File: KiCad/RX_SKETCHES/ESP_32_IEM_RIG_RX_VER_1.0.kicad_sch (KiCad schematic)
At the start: 0 parts

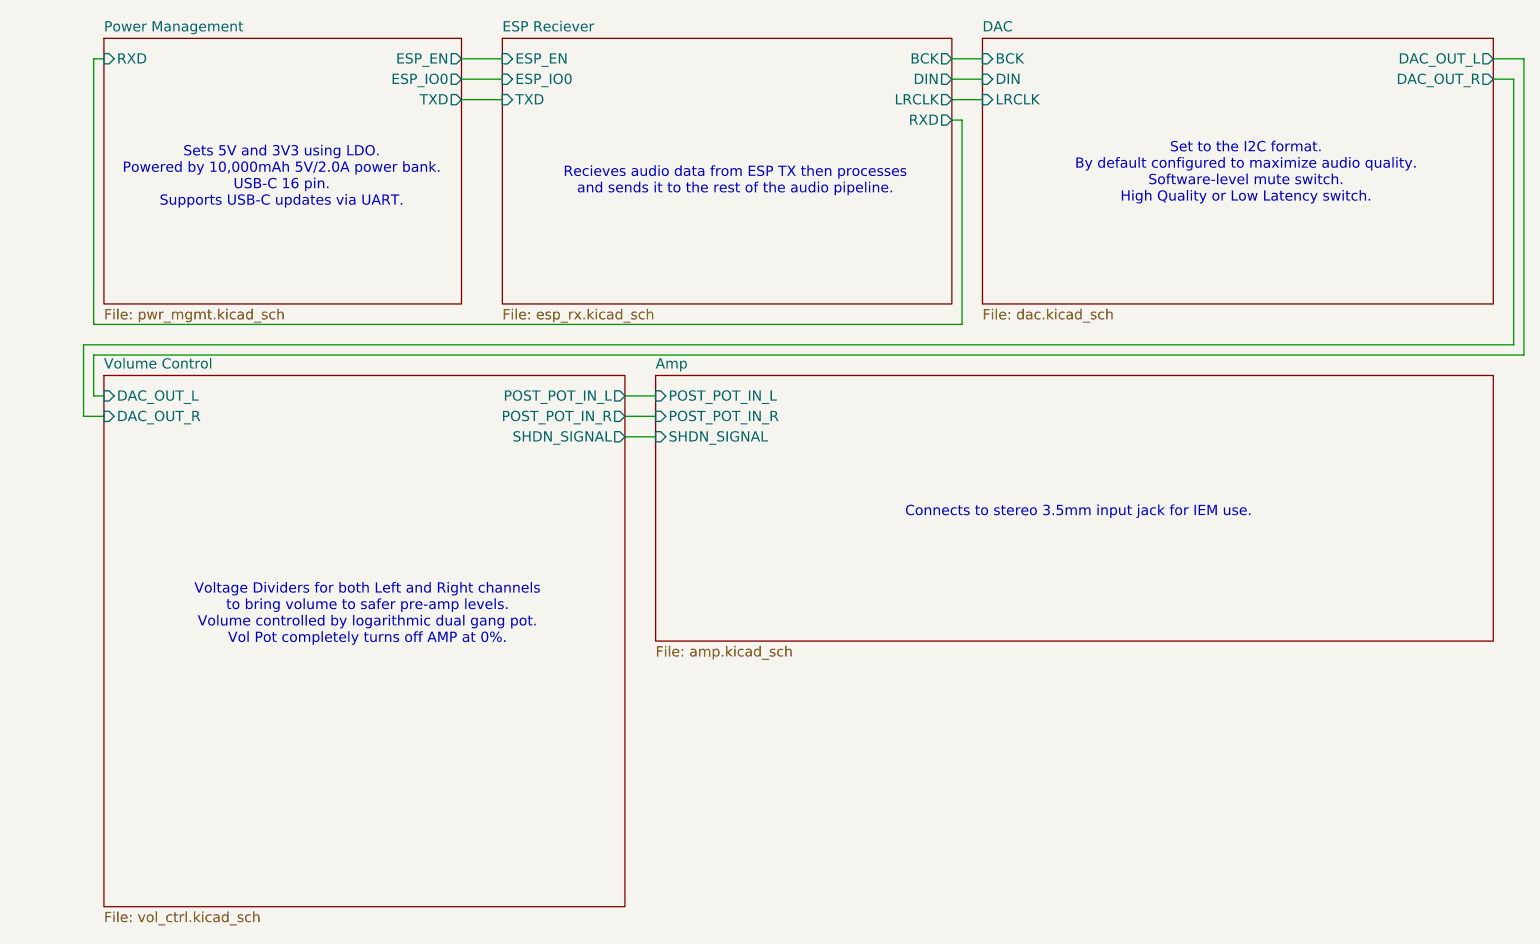
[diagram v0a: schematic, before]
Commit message: Rewire RX hierarchical labels and mark proto DNP parts.
Keep the rotated WROOM-32U and breadboard I2S GPIOs, but attach
ESP_EN/IO0, UART, and BCK/DIN/LRCLK to the pins that actually sit
there after the 270° rotate. Move PCM5102 I2S off FMT/DEMP/XSMT,
put amp shutdown on ~{SHDN}, keep the datasheet 470R+2.2nF filter,
DNP the experimental pot pad and MAX97220A input resistors, and
switch schematic passives to 0805 for hand assembly.

Co-authored-by: luciano <dlmuschamp@users.noreply.github.com>
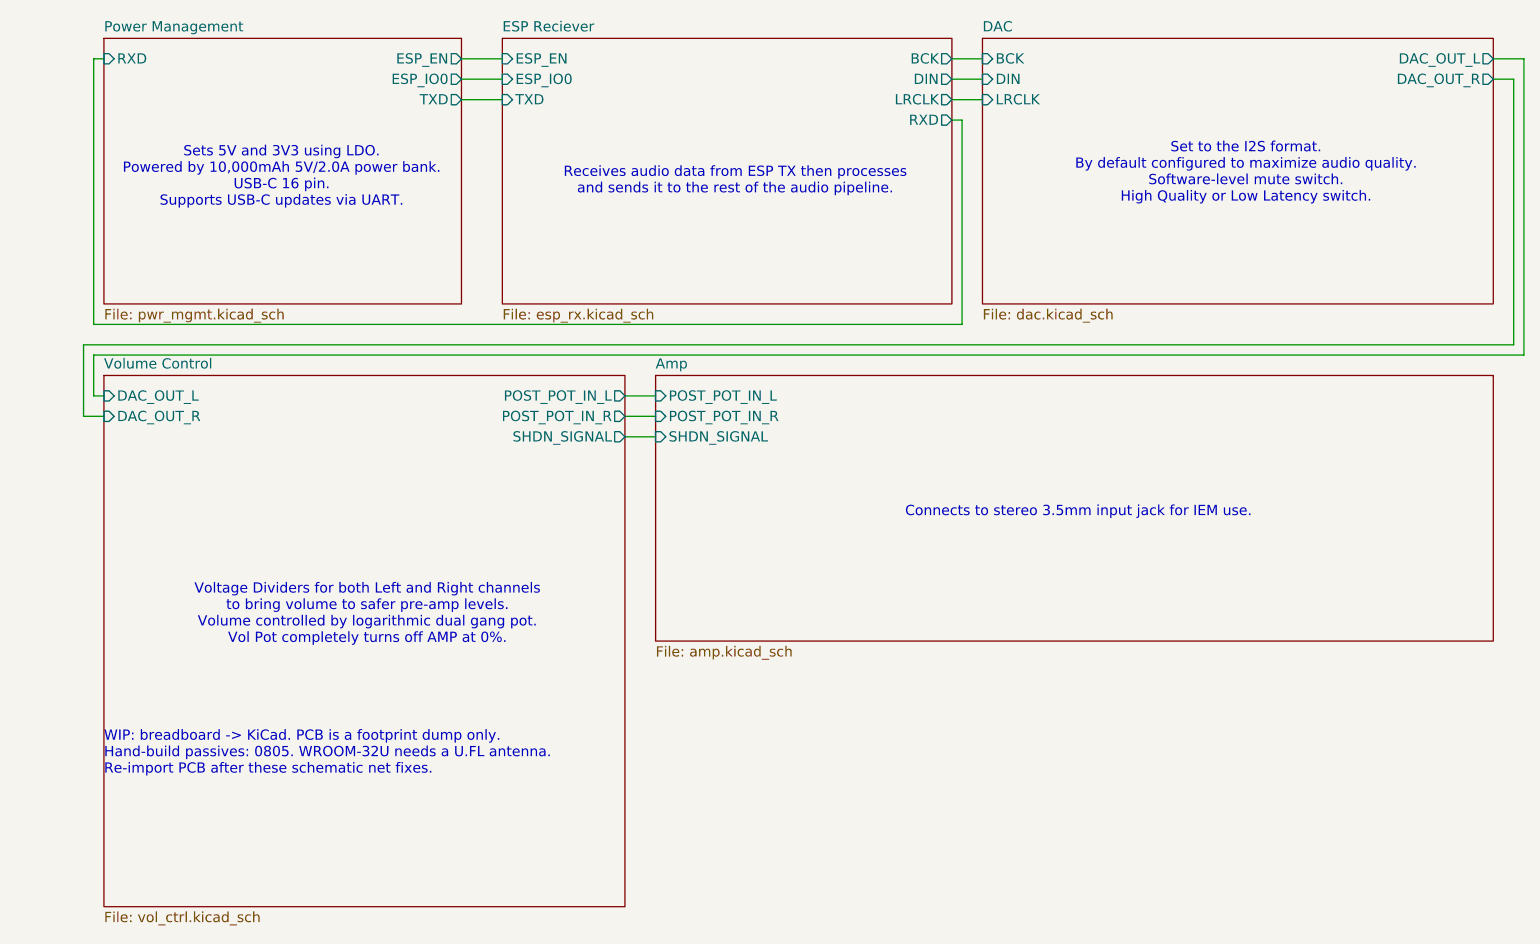
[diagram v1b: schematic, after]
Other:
- note added: "Receives audio data from ESP TX then processes and sends it to the rest of the audio pipeline."
- note added: "Set to the I2S format. By default configured to maximize audio quality. Software-level mute switch. High Quality or Low Latency switch."
- note added: "WIP: breadboard -> KiCad. PCB is a footprint dump only. Hand-build passives: 0805. WROOM-32U needs a U.FL antenna. Re-import PCB after these schematic net fixes."
- note removed: "Recieves audio data from ESP TX then processes and sends it to the rest of the audio pipeline."
- note removed: "Set to the I2C format. By default configured to maximize audio quality. Software-level mute switch. High Quality or Low Latency switch."
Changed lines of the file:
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@@
 		)
 	)
-	(text "Recieves audio data from ESP TX then processes \nand sends it to the rest of the audio pipeline."
+	(text "Receives audio data from ESP TX then processes \nand sends it to the rest of the audio pipeline."
 		(exclude_from_sim no)
 		(at 96.266 39.37 0)
@@
 		)
 	)
-	(text "Set to the I2C format. \nBy default configured to maximize audio quality.\nSoftware-level mute switch.\nHigh Quality or Low Latency switch."
+	(text "Set to the I2S format. \nBy default configured to maximize audio quality.\nSoftware-level mute switch.\nHigh Quality or Low Latency switch."
 		(exclude_from_sim no)
 		(at 159.766 38.354 0)
@@
 		)
 	)
+	(text "WIP: breadboard -> KiCad. PCB is a footprint dump only.\nHand-build passives: 0805. WROOM-32U needs a U.FL antenna.\nRe-import PCB after these schematic net fixes."
+		(exclude_from_sim no)
+		(at 17.78 110.49 0)
+		(effects
+			(font
+				(size 1.27 1.27)
+			)
+			(justify left)
+		)
+	)

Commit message: Document the RX transfer and add ANT1 on the ESP sheet.
Rewrite the README for no display, matching 10,000 mAh USB-C banks
on TX and RX, the firmware I2S map, and first-board KiCad pitfalls.
Place ANT1 as a BOM-only 2.4 GHz U.FL pigtail that mates to the
WROOM-32U module connector (no GPIO, no PCB antenna footprint).

Co-authored-by: luciano <dlmuschamp@users.noreply.github.com>
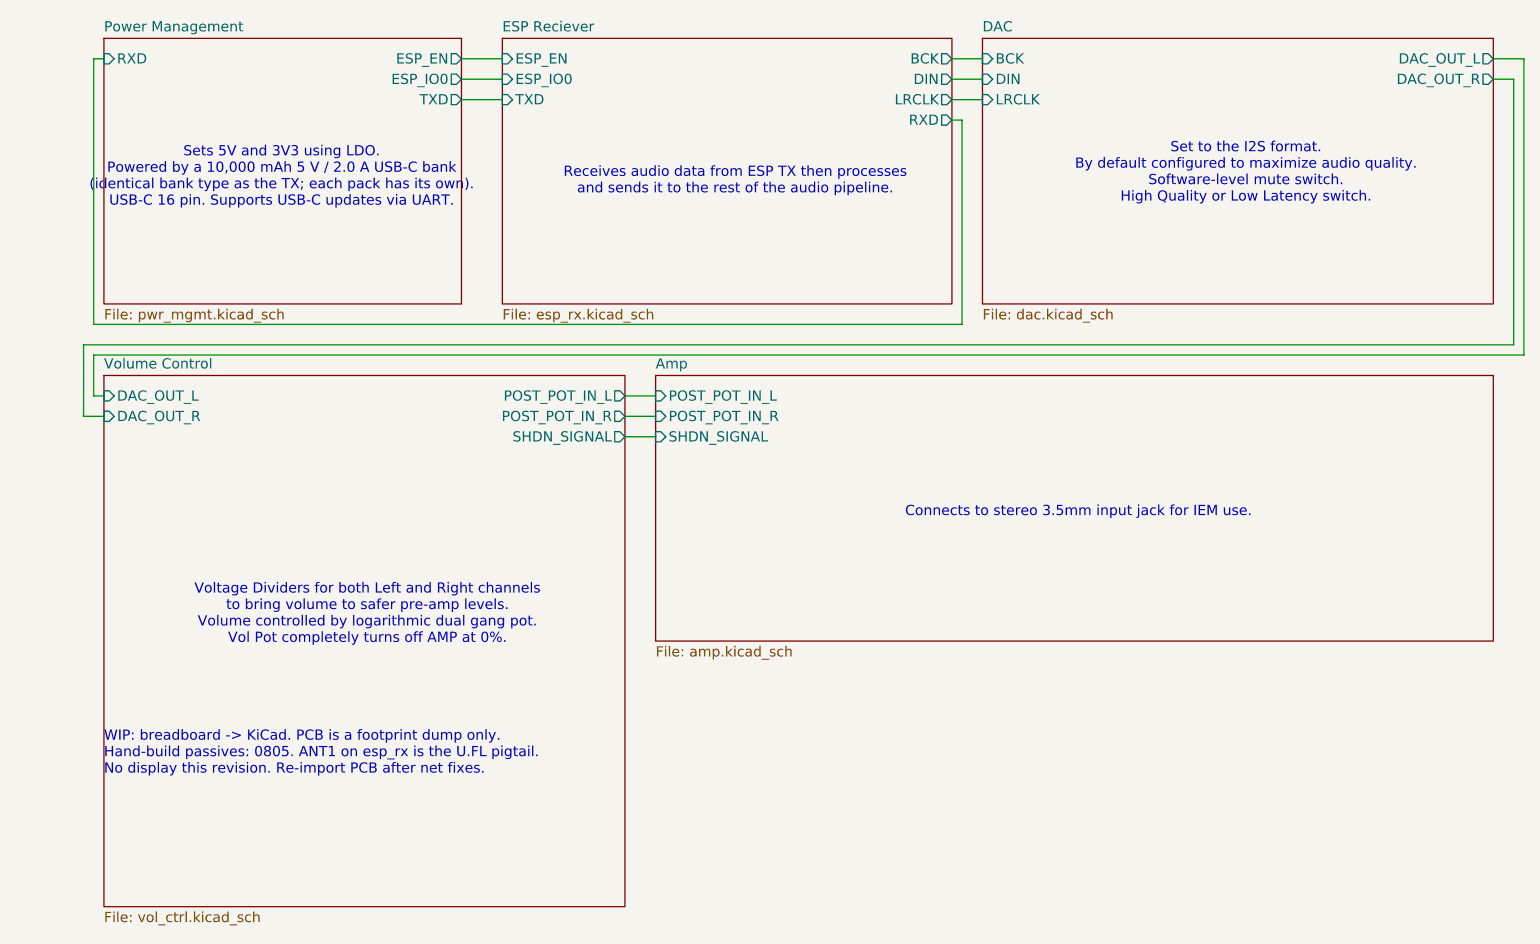
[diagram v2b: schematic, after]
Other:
- note added: "Sets 5V and 3V3 using LDO. Powered by a 10,000 mAh 5 V / 2.0 A USB-C bank (identical bank type as the TX; each pack has its own). USB-C 16 pin. Supports USB-C updates via UART."
- note added: "WIP: breadboard -> KiCad. PCB is a footprint dump only. Hand-build passives: 0805. ANT1 on esp_rx is the U.FL pigtail. No display this revision. Re-import PCB after net fixes."
- note removed: "Sets 5V and 3V3 using LDO. Powered by 10,000mAh 5V/2.0A power bank. USB-C 16 pin. Supports USB-C updates via UART."
- note removed: "WIP: breadboard -> KiCad. PCB is a footprint dump only. Hand-build passives: 0805. WROOM-32U needs a U.FL antenna. Re-import PCB after these schematic net fixes."
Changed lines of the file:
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@@
 		)
 	)
-	(text "Sets 5V and 3V3 using LDO. \nPowered by 10,000mAh 5V/2.0A power bank.\nUSB-C 16 pin. \nSupports USB-C updates via UART."
+	(text "Sets 5V and 3V3 using LDO.\nPowered by a 10,000 mAh 5 V / 2.0 A USB-C bank\n(identical bank type as the TX; each pack has its own).\nUSB-C 16 pin. Supports USB-C updates via UART."
 		(exclude_from_sim no)
 		(at 39.878 38.862 0)
@@
 		)
 	)
-	(text "WIP: breadboard -> KiCad. PCB is a footprint dump only.\nHand-build passives: 0805. WROOM-32U needs a U.FL antenna.\nRe-import PCB after these schematic net fixes."
+	(text "WIP: breadboard -> KiCad. PCB is a footprint dump only.\nHand-build passives: 0805. ANT1 on esp_rx is the U.FL pigtail.\nNo display this revision. Re-import PCB after net fixes."
 		(exclude_from_sim no)
 		(at 17.78 110.49 0)

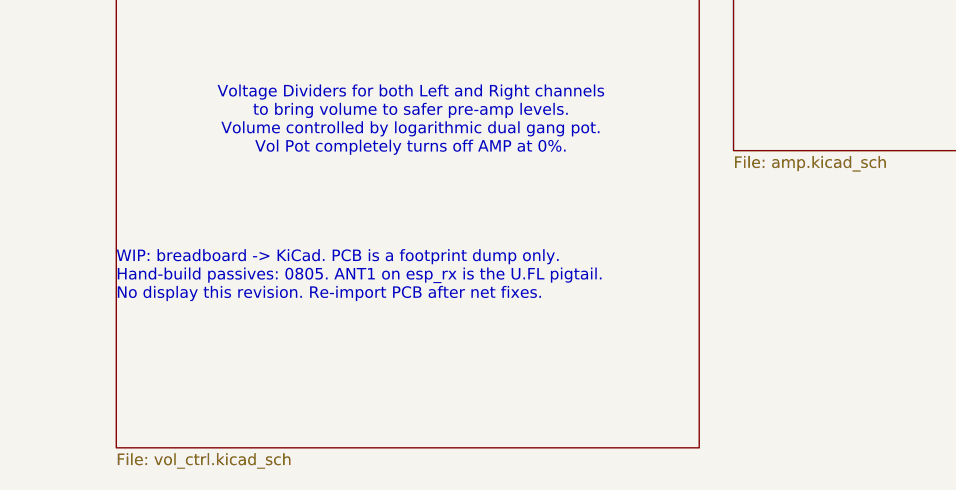
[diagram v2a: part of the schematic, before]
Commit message: Align RX passives and analog nets with the part datasheets.
Put every R/C on the 0805 HandSolder footprint. Rewire the PCM5102
470R filter onto OUTL/OUTR, decouple LDOO, and land the flying cap
on CAPP/CAPM. Move the headphone jack off PVSS/SVSS onto OUTL/OUTR
with a PVSS hold cap. Tie CP2102C VIO to VDD, pull RST up, add the
LM3940 0.47uF Cin, and pull IO0 up for normal boot.

Co-authored-by: luciano <dlmuschamp@users.noreply.github.com>
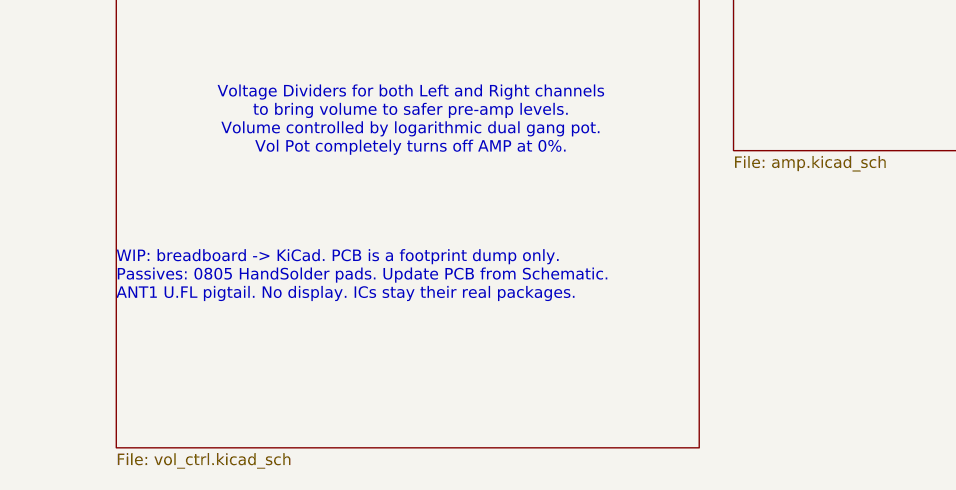
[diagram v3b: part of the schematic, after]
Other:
- note added: "WIP: breadboard -> KiCad. PCB is a footprint dump only. Passives: 0805 HandSolder pads. Update PCB from Schematic. ANT1 U.FL pigtail. No display. ICs stay their real packages."
- note removed: "WIP: breadboard -> KiCad. PCB is a footprint dump only. Hand-build passives: 0805. ANT1 on esp_rx is the U.FL pigtail. No display this revision. Re-import PCB after net fixes."
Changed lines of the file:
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@@
 		)
 	)
-	(text "WIP: breadboard -> KiCad. PCB is a footprint dump only.\nHand-build passives: 0805. ANT1 on esp_rx is the U.FL pigtail.\nNo display this revision. Re-import PCB after net fixes."
+	(text "WIP: breadboard -> KiCad. PCB is a footprint dump only.\nPassives: 0805 HandSolder pads. Update PCB from Schematic.\nANT1 U.FL pigtail. No display. ICs stay their real packages."
 		(exclude_from_sim no)
 		(at 17.78 110.49 0)
